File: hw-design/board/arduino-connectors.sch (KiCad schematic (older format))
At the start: 15 parts, among them P1 Power, P2 Analog, P3 Digital, P4 Digital, P5 Hole, P6 Hole, P7 Hole, P8 Hole, Q1 2N7002

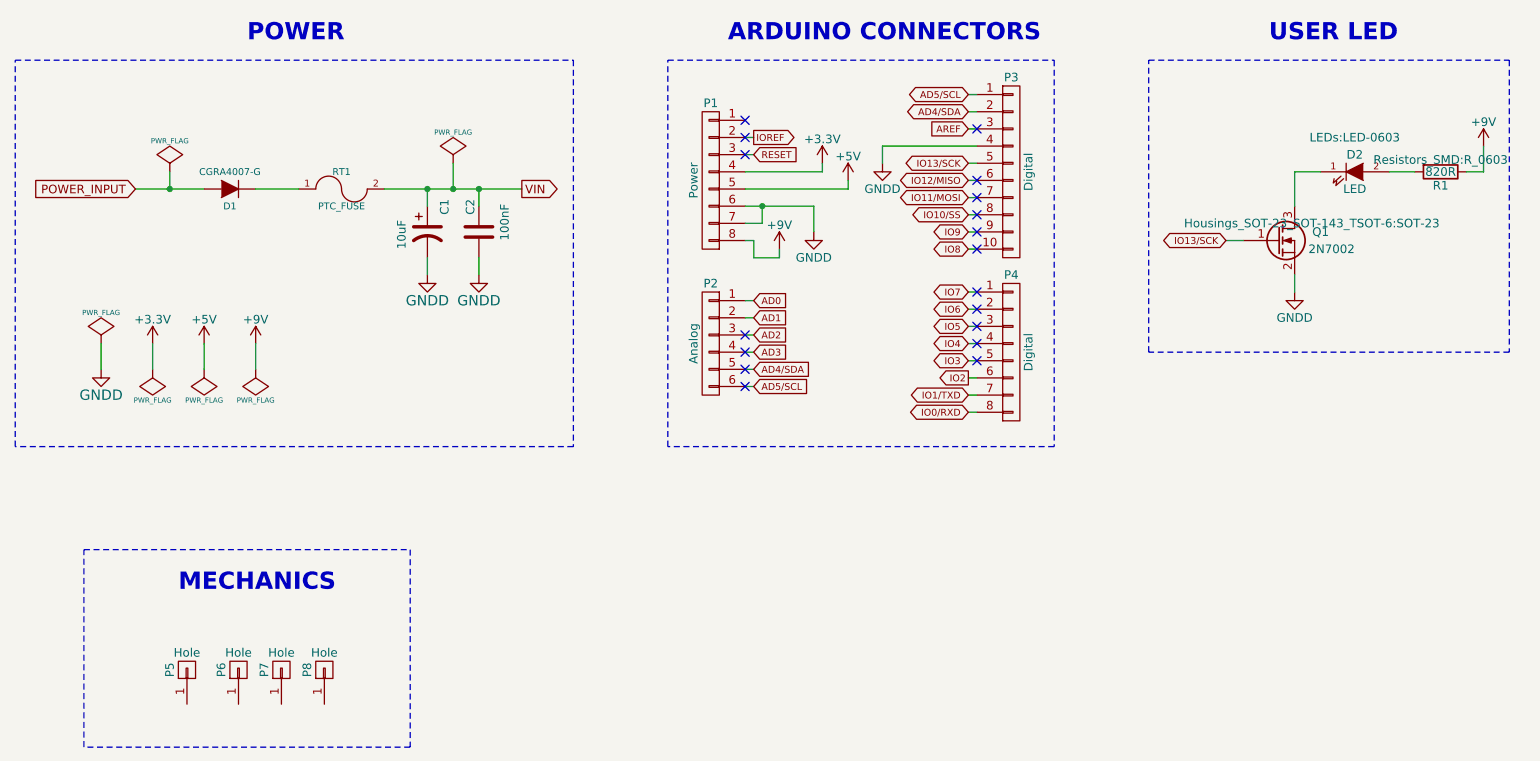
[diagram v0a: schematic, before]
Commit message: sch: changing input voltage from +9V to +12V
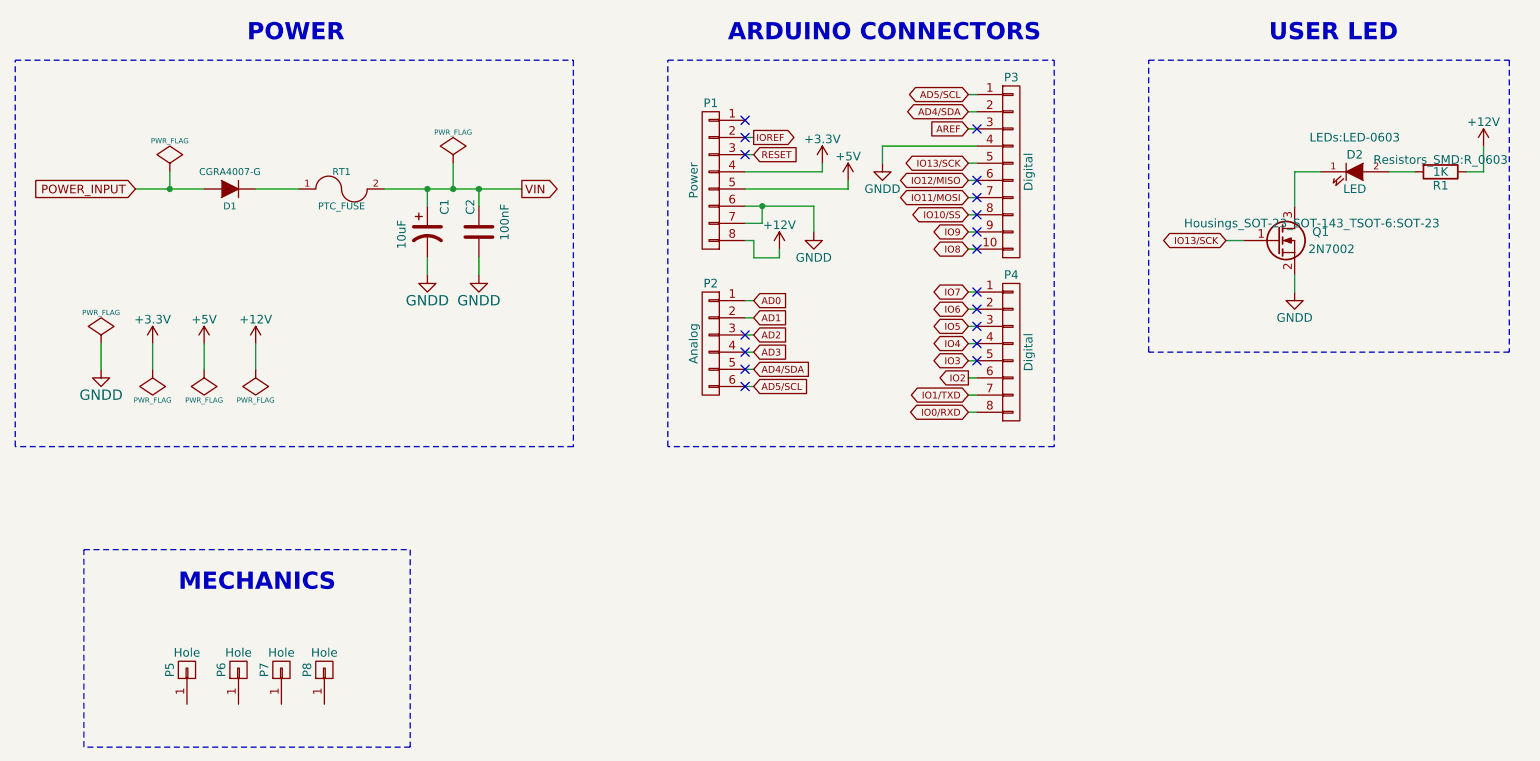
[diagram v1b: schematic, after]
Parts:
- R1: value 820R -> 1K; MPN ESR03EZPJ821 -> ESR03EZPJ102
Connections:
- net +9V renamed +12V
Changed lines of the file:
@@
 	-1   0    0    1
-$EndComp
-$Comp
-L +9V #PWR010
-U 1 1 557B43C7
-P 2800 2950
-F 0 "#PWR010" H 2800 2800 50  0001 C CNN
-F 1 "+9V" H 2800 3090 50  0000 C CNN
-F 2 "" H 2800 2950 60  0000 C CNN
-F 3 "" H 2800 2950 60  0000 C CNN
-	1    2800 2950
-	1    0    0    -1
 $EndComp
 Text GLabel 2100 2050 0    50   Input ~ 0
@@
 P 9700 1950
 F 0 "R1" V 9780 1950 50  0000 C CNN
-F 1 "820R" V 9700 1950 50  0000 C CNN
+F 1 "1K" V 9700 1950 50  0000 C CNN
 F 2 "Resistors_SMD:R_0603" V 9630 1950 50  0000 C CNN
 F 3 "" H 9700 1950 30  0000 C CNN
-F 4 "ESR03EZPJ821" V 9700 1950 60  0001 C CNN "MPN"
+F 4 "ESR03EZPJ102" V 9700 1950 60  0001 C CNN "MPN"
 	1    9700 1950
 	0    1    1    0
@@
 Wire Wire Line
 	9550 1950 9400 1950
-$Comp
-L +9V #PWR012
-U 1 1 558C6BA4
-P 9950 1800
-F 0 "#PWR012" H 9950 1650 50  0001 C CNN
-F 1 "+9V" H 9950 1940 50  0000 C CNN
-F 2 "" H 9950 1800 60  0000 C CNN
-F 3 "" H 9950 1800 60  0000 C CNN
-	1    9950 1800
-	1    0    0    -1
-$EndComp
 Wire Wire Line
 	9850 1950 9950 1950
@@
 	5750 2250 5750 2150
 Connection ~ 5750 2150
-$Comp
-L +9V #PWR017
-U 1 1 558D2217
-P 5850 2400
-F 0 "#PWR017" H 5850 2250 50  0001 C CNN
-F 1 "+9V" H 5850 2540 50  0000 C CNN
-F 2 "" H 5850 2400 60  0000 C CNN
-F 3 "" H 5850 2400 60  0000 C CNN
-	1    5850 2400
-	1    0    0    -1
-$EndComp
 Wire Wire Line
 	5650 2350 5700 2350
@@
 Wire Notes Line
 	1800 5300 1800 4150
+$Comp
+L +12V #PWR?
+U 1 1 560AD010
+P 2800 2950
+F 0 "#PWR?" H 2800 2800 50  0001 C CNN
+F 1 "+12V" H 2800 3090 50  0000 C CNN
+F 2 "" H 2800 2950 60  0000 C CNN
+F 3 "" H 2800 2950 60  0000 C CNN
+	1    2800 2950
+	1    0    0    -1
+$EndComp
+$Comp
+L +12V #PWR?
+U 1 1 560ADCC7
+P 5850 2400
+F 0 "#PWR?" H 5850 2250 50  0001 C CNN
+F 1 "+12V" H 5850 2540 50  0000 C CNN
+F 2 "" H 5850 2400 60  0000 C CNN
+F 3 "" H 5850 2400 60  0000 C CNN
+	1    5850 2400
+	1    0    0    -1
+$EndComp
+$Comp
+L +12V #PWR?
+U 1 1 560AEADC
+P 9950 1800
+F 0 "#PWR?" H 9950 1650 50  0001 C CNN
+F 1 "+12V" H 9950 1940 50  0000 C CNN
+F 2 "" H 9950 1800 60  0000 C CNN
+F 3 "" H 9950 1800 60  0000 C CNN
+	1    9950 1800
+	1    0    0    -1
+$EndComp
 $EndSCHEMATC

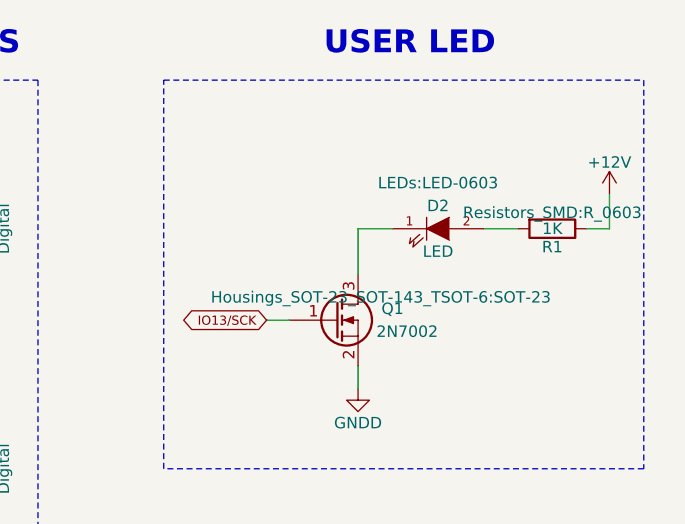
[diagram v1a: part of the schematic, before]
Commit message: sch: fixing MOSFET + new BOM exported
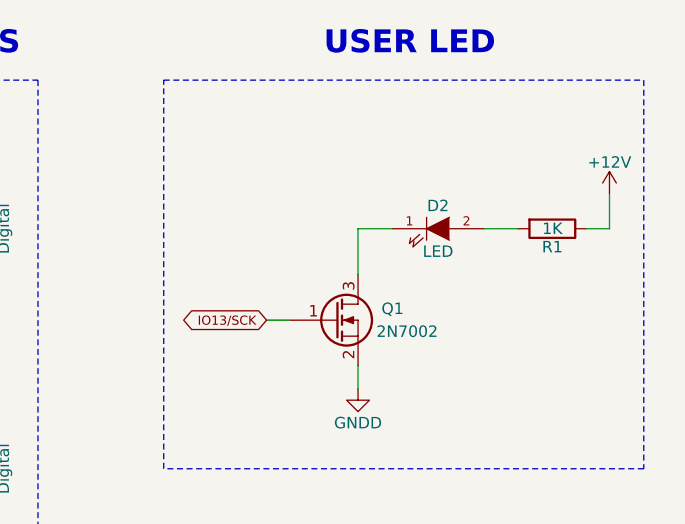
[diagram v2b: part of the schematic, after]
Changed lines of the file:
@@
 F 0 "Q1" H 9050 2400 50  0000 R CNN
 F 1 "2N7002" H 9200 2300 50  0000 R CNN
-F 2 "Housings_SOT-23_SOT-143_TSOT-6:SOT-23" H 8950 2450 50  0000 C CNN
+F 2 "Housings_SOT-23_SOT-143_TSOT-6:SOT-23" H 8950 2450 50  0001 C CNN
 F 3 "" H 8750 2350 60  0000 C CNN
 F 4 "2N7002P,215" H 8750 2350 60  0001 C CNN "MPN"
@@
 $EndComp
 $Comp
-L GNDD #PWR011
+L GNDD #PWR010
 U 1 1 558C6089
 P 8850 2650
-F 0 "#PWR011" H 8850 2400 50  0001 C CNN
+F 0 "#PWR010" H 8850 2400 50  0001 C CNN
 F 1 "GNDD" H 8850 2500 50  0000 C CNN
 F 2 "" H 8850 2650 60  0000 C CNN
@@
 F 0 "D2" H 9200 2050 50  0000 C CNN
 F 1 "LED" H 9200 1850 50  0000 C CNN
-F 2 "LEDs:LED-0603" H 9200 2150 50  0000 C CNN
+F 2 "LEDs:LED-0603" H 9200 2150 50  0001 C CNN
 F 3 "" H 9200 1950 60  0000 C CNN
 F 4 "LS Q976-NR-1" H 9200 1950 60  0001 C CNN "MPN"
@@
 F 0 "R1" V 9780 1950 50  0000 C CNN
 F 1 "1K" V 9700 1950 50  0000 C CNN
-F 2 "Resistors_SMD:R_0603" V 9630 1950 50  0000 C CNN
+F 2 "Resistors_SMD:R_0603" V 9630 1950 50  0001 C CNN
 F 3 "" H 9700 1950 30  0000 C CNN
 F 4 "ESR03EZPJ102" V 9700 1950 60  0001 C CNN "MPN"
@@
 	8000 3000 8000 1300
 $Comp
-L PWR_FLAG #FLG013
+L PWR_FLAG #FLG011
 U 1 1 558CC3E6
 P 2200 3100
-F 0 "#FLG013" H 2200 3195 30  0001 C CNN
+F 0 "#FLG011" H 2200 3195 30  0001 C CNN
 F 1 "PWR_FLAG" H 2200 3280 30  0000 C CNN
 F 2 "" H 2200 3100 60  0000 C CNN
@@
 	2200 2950 2200 3100
 $Comp
-L +3.3V #PWR014
+L +3.3V #PWR012
 U 1 1 558CC417
 P 2200 2950
-F 0 "#PWR014" H 2200 2800 50  0001 C CNN
+F 0 "#PWR012" H 2200 2800 50  0001 C CNN
 F 1 "+3.3V" H 2200 3090 50  0000 C CNN
 F 2 "" H 2200 2950 60  0000 C CNN
@@
 NoConn ~ 7000 1700
 $Comp
-L GNDD #PWR015
+L GNDD #PWR013
 U 1 1 558D1E0A
 P 6450 1900
-F 0 "#PWR015" H 6450 1650 50  0001 C CNN
+F 0 "#PWR013" H 6450 1650 50  0001 C CNN
 F 1 "GNDD" H 6450 1750 50  0000 C CNN
 F 2 "" H 6450 1900 60  0000 C CNN
@@
 	6450 1800 7000 1800
 $Comp
-L GNDD #PWR016
+L GNDD #PWR014
 U 1 1 558D2084
 P 6050 2300
-F 0 "#PWR016" H 6050 2050 50  0001 C CNN
+F 0 "#PWR014" H 6050 2050 50  0001 C CNN
 F 1 "GNDD" H 6050 2150 50  0000 C CNN
 F 2 "" H 6050 2300 60  0000 C CNN
@@
 	5850 2450 5850 2400
 $Comp
-L +5V #PWR018
+L +5V #PWR015
 U 1 1 558D2AB4
 P 6250 2000
-F 0 "#PWR018" H 6250 1850 50  0001 C CNN
+F 0 "#PWR015" H 6250 1850 50  0001 C CNN
 F 1 "+5V" H 6250 2140 50  0000 C CNN
 F 2 "" H 6250 2000 60  0000 C CNN
@@
 	6250 2050 6250 2000
 $Comp
-L +3.3V #PWR019
+L +3.3V #PWR016
 U 1 1 558D2EDB
 P 6100 1900
-F 0 "#PWR019" H 6100 1750 50  0001 C CNN
+F 0 "#PWR016" H 6100 1750 50  0001 C CNN
 F 1 "+3.3V" H 6100 2040 50  0000 C CNN
 F 2 "" H 6100 1900 60  0000 C CNN
@@
 	1800 5300 1800 4150
 $Comp
-L +12V #PWR?
+L +12V #PWR017
 U 1 1 560AD010
 P 2800 2950
-F 0 "#PWR?" H 2800 2800 50  0001 C CNN
+F 0 "#PWR017" H 2800 2800 50  0001 C CNN
 F 1 "+12V" H 2800 3090 50  0000 C CNN
 F 2 "" H 2800 2950 60  0000 C CNN
@@
 $EndComp
 $Comp
-L +12V #PWR?
+L +12V #PWR018
 U 1 1 560ADCC7
 P 5850 2400
-F 0 "#PWR?" H 5850 2250 50  0001 C CNN
+F 0 "#PWR018" H 5850 2250 50  0001 C CNN
 F 1 "+12V" H 5850 2540 50  0000 C CNN
 F 2 "" H 5850 2400 60  0000 C CNN
@@
 $EndComp
 $Comp
-L +12V #PWR?
+L +12V #PWR019
 U 1 1 560AEADC
 P 9950 1800
-F 0 "#PWR?" H 9950 1650 50  0001 C CNN
+F 0 "#PWR019" H 9950 1650 50  0001 C CNN
 F 1 "+12V" H 9950 1940 50  0000 C CNN
 F 2 "" H 9950 1800 60  0000 C CNN

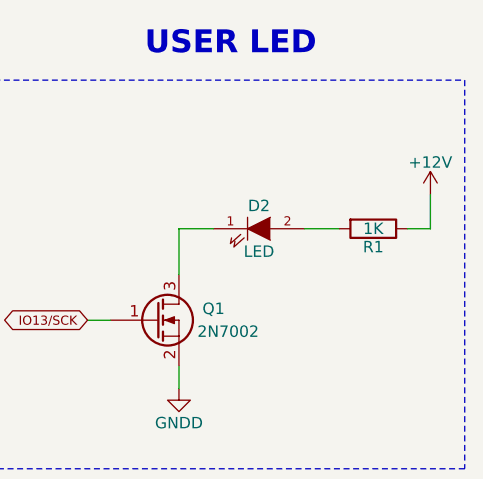
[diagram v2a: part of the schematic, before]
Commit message: fixing user led voltage
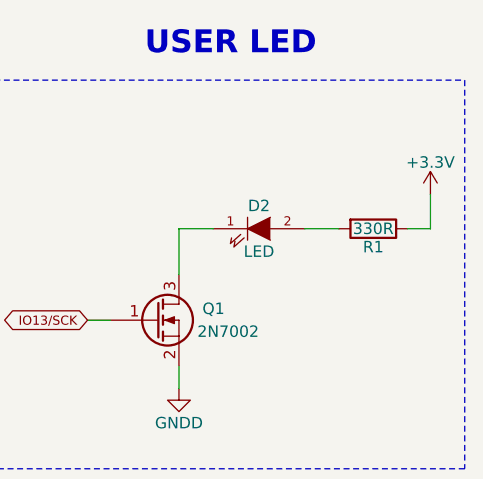
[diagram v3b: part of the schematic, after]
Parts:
- R1: value 1K -> 330R; MPN ESR03EZPJ102 -> RMCF0603JT330R
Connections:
- net +12V: no longer R1.1
- net +3V3: now also R1.1
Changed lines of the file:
@@
 P 9700 1950
 F 0 "R1" V 9780 1950 50  0000 C CNN
-F 1 "1K" V 9700 1950 50  0000 C CNN
+F 1 "330R" V 9700 1950 50  0000 C CNN
 F 2 "Resistors_SMD:R_0603" V 9630 1950 50  0001 C CNN
 F 3 "" H 9700 1950 30  0000 C CNN
-F 4 "ESR03EZPJ102" V 9700 1950 60  0001 C CNN "MPN"
+F 4 "RMCF0603JT330R" V 9700 1950 60  0001 C CNN "MPN"
 	1    9700 1950
 	0    1    1    0
@@
 $EndComp
 $Comp
-L +12V #PWR019
-U 1 1 560AEADC
+L +3.3V #PWR?
+U 1 1 5622A80C
 P 9950 1800
-F 0 "#PWR019" H 9950 1650 50  0001 C CNN
-F 1 "+12V" H 9950 1940 50  0000 C CNN
+F 0 "#PWR?" H 9950 1650 50  0001 C CNN
+F 1 "+3.3V" H 9950 1940 50  0000 C CNN
 F 2 "" H 9950 1800 60  0000 C CNN
 F 3 "" H 9950 1800 60  0000 C CNN

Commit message: fix all DRC issues
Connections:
- net +12V: no longer P1.8 (P8)
- net VIN: now also P1.8 (P8)
- no-connect marks 18 -> 5
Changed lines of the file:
@@
 $EndComp
 $Comp
-L PWR_FLAG #FLG01
+L PWR_FLAG #FLG1
 U 1 1 54B500E8
 P 1900 2950
-F 0 "#FLG01" H 1900 3045 30  0001 C CNN
+F 0 "#FLG1" H 1900 3045 30  0001 C CNN
 F 1 "PWR_FLAG" H 1900 3130 30  0000 C CNN
 F 2 "" H 1900 2950 60  0000 C CNN
@@
 $EndComp
 $Comp
-L PWR_FLAG #FLG02
+L PWR_FLAG #FLG3
 U 1 1 54B50E4C
 P 2300 1950
-F 0 "#FLG02" H 2300 2045 30  0001 C CNN
+F 0 "#FLG3" H 2300 2045 30  0001 C CNN
 F 1 "PWR_FLAG" H 2300 2130 30  0000 C CNN
 F 2 "" H 2300 1950 60  0000 C CNN
@@
 $EndComp
 $Comp
-L GNDD #PWR03
+L GNDD #PWR1
 U 1 1 54E7EDE1
 P 1900 3100
-F 0 "#PWR03" H 1900 2850 60  0001 C CNN
+F 0 "#PWR1" H 1900 2850 60  0001 C CNN
 F 1 "GNDD" H 1900 2950 60  0000 C CNN
 F 2 "" H 1900 3100 60  0000 C CNN
@@
 $EndComp
 $Comp
-L GNDD #PWR04
+L GNDD #PWR17
 U 1 1 54E7EE6C
 P 3800 2550
-F 0 "#PWR04" H 3800 2300 60  0001 C CNN
+F 0 "#PWR17" H 3800 2300 60  0001 C CNN
 F 1 "GNDD" H 3800 2400 60  0000 C CNN
 F 2 "" H 3800 2550 60  0000 C CNN
@@
 $EndComp
 $Comp
-L GNDD #PWR05
+L GNDD #PWR18
 U 1 1 54E7EE80
 P 4100 2550
-F 0 "#PWR05" H 4100 2300 60  0001 C CNN
+F 0 "#PWR18" H 4100 2300 60  0001 C CNN
 F 1 "GNDD" H 4100 2400 60  0000 C CNN
 F 2 "" H 4100 2550 60  0000 C CNN
@@
 $EndComp
 $Comp
-L PWR_FLAG #FLG06
+L PWR_FLAG #FLG6
 U 1 1 557B2C54
 P 3950 1900
-F 0 "#FLG06" H 3950 1995 30  0001 C CNN
+F 0 "#FLG6" H 3950 1995 30  0001 C CNN
 F 1 "PWR_FLAG" H 3950 2080 30  0000 C CNN
 F 2 "" H 3950 1900 60  0000 C CNN
@@
 $EndComp
 $Comp
-L PWR_FLAG #FLG07
+L PWR_FLAG #FLG4
 U 1 1 557B3123
 P 2500 3100
-F 0 "#FLG07" H 2500 3195 30  0001 C CNN
+F 0 "#FLG4" H 2500 3195 30  0001 C CNN
 F 1 "PWR_FLAG" H 2500 3280 30  0000 C CNN
 F 2 "" H 2500 3100 60  0000 C CNN
@@
 $EndComp
 $Comp
-L +5V #PWR08
+L +5V #PWR8
 U 1 1 557B3200
 P 2500 2950
-F 0 "#PWR08" H 2500 2800 50  0001 C CNN
+F 0 "#PWR8" H 2500 2800 50  0001 C CNN
 F 1 "+5V" H 2500 3090 50  0000 C CNN
 F 2 "" H 2500 2950 60  0000 C CNN
@@
 $EndComp
 $Comp
-L PWR_FLAG #FLG09
+L PWR_FLAG #FLG5
 U 1 1 557B4378
 P 2800 3100
-F 0 "#FLG09" H 2800 3195 30  0001 C CNN
+F 0 "#FLG5" H 2800 3195 30  0001 C CNN
 F 1 "PWR_FLAG" H 2800 3280 30  0000 C CNN
 F 2 "" H 2800 3100 60  0000 C CNN
@@
 $EndComp
 $Comp
-L GNDD #PWR010
+L GNDD #PWR36
 U 1 1 558C6089
 P 8850 2650
-F 0 "#PWR010" H 8850 2400 50  0001 C CNN
+F 0 "#PWR36" H 8850 2400 50  0001 C CNN
 F 1 "GNDD" H 8850 2500 50  0000 C CNN
 F 2 "" H 8850 2650 60  0000 C CNN
@@
 	8000 3000 8000 1300
 $Comp
-L PWR_FLAG #FLG011
+L PWR_FLAG #FLG2
 U 1 1 558CC3E6
 P 2200 3100
-F 0 "#FLG011" H 2200 3195 30  0001 C CNN
+F 0 "#FLG2" H 2200 3195 30  0001 C CNN
 F 1 "PWR_FLAG" H 2200 3280 30  0000 C CNN
 F 2 "" H 2200 3100 60  0000 C CNN
@@
 	2200 2950 2200 3100
 $Comp
-L +3.3V #PWR012
+L +3.3V #PWR5
 U 1 1 558CC417
 P 2200 2950
-F 0 "#PWR012" H 2200 2800 50  0001 C CNN
+F 0 "#PWR5" H 2200 2800 50  0001 C CNN
 F 1 "+3.3V" H 2200 3090 50  0000 C CNN
 F 2 "" H 2200 2950 60  0000 C CNN
@@
 	1    0    0    -1
 $EndComp
-NoConn ~ 5650 1750
-NoConn ~ 5650 1850
-NoConn ~ 5650 2900
-NoConn ~ 5650 3000
-NoConn ~ 5650 3100
-NoConn ~ 5650 3200
-NoConn ~ 7000 3050
-NoConn ~ 7000 2950
-NoConn ~ 7000 2850
-NoConn ~ 7000 2750
-NoConn ~ 7000 2650
-NoConn ~ 7000 2400
-NoConn ~ 7000 2300
-NoConn ~ 7000 2200
-NoConn ~ 7000 2100
-NoConn ~ 7000 2000
-NoConn ~ 7000 1700
-$Comp
-L GNDD #PWR013
+$Comp
+L GNDD #PWR28
 U 1 1 558D1E0A
 P 6450 1900
-F 0 "#PWR013" H 6450 1650 50  0001 C CNN
+F 0 "#PWR28" H 6450 1650 50  0001 C CNN
 F 1 "GNDD" H 6450 1750 50  0000 C CNN
 F 2 "" H 6450 1900 60  0000 C CNN
@@
 	6450 1800 7000 1800
 $Comp
-L GNDD #PWR014
+L GNDD #PWR25
 U 1 1 558D2084
 P 6050 2300
-F 0 "#PWR014" H 6050 2050 50  0001 C CNN
+F 0 "#PWR25" H 6050 2050 50  0001 C CNN
 F 1 "GNDD" H 6050 2150 50  0000 C CNN
 F 2 "" H 6050 2300 60  0000 C CNN
@@
 Wire Wire Line
 	5650 2350 5700 2350
-Wire Wire Line
-	5700 2350 5700 2450
-Wire Wire Line
-	5700 2450 5850 2450
-Wire Wire Line
-	5850 2450 5850 2400
-$Comp
-L +5V #PWR015
+$Comp
+L +5V #PWR27
 U 1 1 558D2AB4
 P 6250 2000
-F 0 "#PWR015" H 6250 1850 50  0001 C CNN
+F 0 "#PWR27" H 6250 1850 50  0001 C CNN
 F 1 "+5V" H 6250 2140 50  0000 C CNN
 F 2 "" H 6250 2000 60  0000 C CNN
@@
 	6250 2050 6250 2000
 $Comp
-L +3.3V #PWR016
+L +3.3V #PWR26
 U 1 1 558D2EDB
 P 6100 1900
-F 0 "#PWR016" H 6100 1750 50  0001 C CNN
+F 0 "#PWR26" H 6100 1750 50  0001 C CNN
 F 1 "+3.3V" H 6100 2040 50  0000 C CNN
 F 2 "" H 6100 1900 60  0000 C CNN
@@
 	1800 5300 1800 4150
 $Comp
-L +12V #PWR017
+L +12V #PWR14
 U 1 1 560AD010
 P 2800 2950
-F 0 "#PWR017" H 2800 2800 50  0001 C CNN
+F 0 "#PWR14" H 2800 2800 50  0001 C CNN
 F 1 "+12V" H 2800 3090 50  0000 C CNN
 F 2 "" H 2800 2950 60  0000 C CNN
@@
 $EndComp
 $Comp
-L +12V #PWR018
-U 1 1 560ADCC7
-P 5850 2400
-F 0 "#PWR018" H 5850 2250 50  0001 C CNN
-F 1 "+12V" H 5850 2540 50  0000 C CNN
-F 2 "" H 5850 2400 60  0000 C CNN
-F 3 "" H 5850 2400 60  0000 C CNN
-	1    5850 2400
-	1    0    0    -1
-$EndComp
-$Comp
-L +3.3V #PWR?
+L +3.3V #PWR38
 U 1 1 5622A80C
 P 9950 1800
-F 0 "#PWR?" H 9950 1650 50  0001 C CNN
+F 0 "#PWR38" H 9950 1650 50  0001 C CNN
 F 1 "+3.3V" H 9950 1940 50  0000 C CNN
 F 2 "" H 9950 1800 60  0000 C CNN
@@
 	1    0    0    -1
 $EndComp
+NoConn ~ 2400 5050
+NoConn ~ 2700 5050
+NoConn ~ 2950 5050
+NoConn ~ 3200 5050
+Text GLabel 5700 2350 2    50   Input ~ 0
+VIN
 $EndSCHEMATC

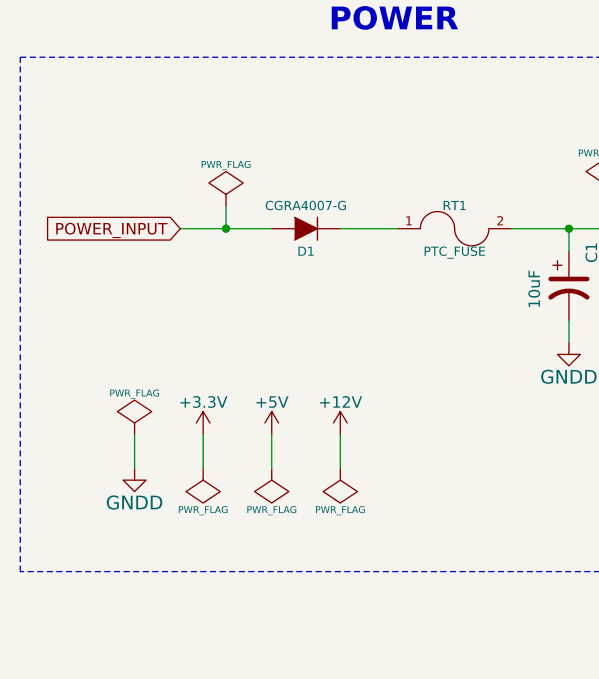
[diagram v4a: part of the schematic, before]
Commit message: connect all voltage inputs pins
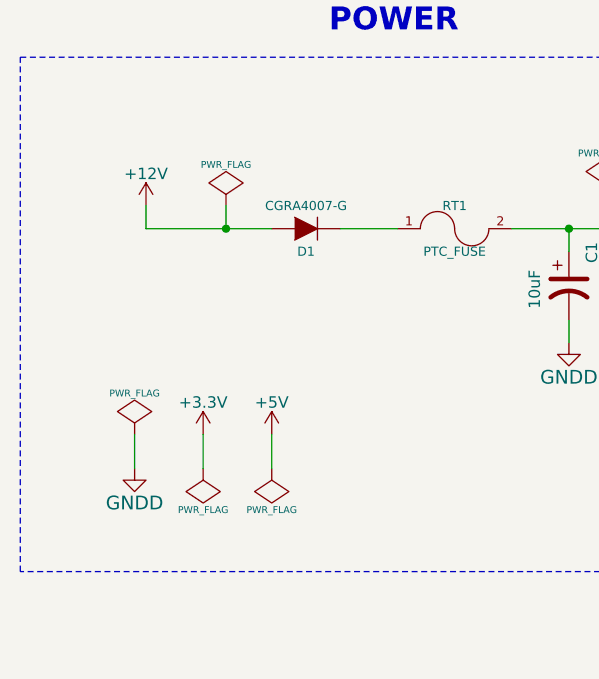
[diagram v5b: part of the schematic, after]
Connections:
- net POWER_INPUT is gone; now on net +12V: D1.2 (A)
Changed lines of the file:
@@
 	1    0    0    -1
 $EndComp
-$Comp
-L PWR_FLAG #FLG5
-U 1 1 557B4378
-P 2800 3100
-F 0 "#FLG5" H 2800 3195 30  0001 C CNN
-F 1 "PWR_FLAG" H 2800 3280 30  0000 C CNN
-F 2 "" H 2800 3100 60  0000 C CNN
-F 3 "" H 2800 3100 60  0000 C CNN
-	1    2800 3100
-	-1   0    0    1
-$EndComp
-Text GLabel 2100 2050 0    50   Input ~ 0
-POWER_INPUT
 Text Notes 2750 1200 0    100  ~ 20
 POWER
@@
 	2800 2050 3050 2050
 Wire Wire Line
-	2100 2050 2500 2050
+	1950 2050 2500 2050
 Wire Wire Line
 	1900 2950 1900 3100
@@
 Wire Wire Line
 	2500 2950 2500 3100
-Wire Wire Line
-	2800 2950 2800 3100
 Connection ~ 3800 2050
 Connection ~ 4100 2050
@@
 L +12V #PWR14
 U 1 1 560AD010
-P 2800 2950
-F 0 "#PWR14" H 2800 2800 50  0001 C CNN
-F 1 "+12V" H 2800 3090 50  0000 C CNN
-F 2 "" H 2800 2950 60  0000 C CNN
-F 3 "" H 2800 2950 60  0000 C CNN
-	1    2800 2950
+P 1950 1950
+F 0 "#PWR14" H 1950 1800 50  0001 C CNN
+F 1 "+12V" H 1950 2090 50  0000 C CNN
+F 2 "" H 1950 1950 60  0000 C CNN
+F 3 "" H 1950 1950 60  0000 C CNN
+	1    1950 1950
 	1    0    0    -1
 $EndComp
@@
 Text GLabel 5700 2350 2    50   Input ~ 0
 VIN
+Wire Wire Line
+	1950 2050 1950 1950
 $EndSCHEMATC
